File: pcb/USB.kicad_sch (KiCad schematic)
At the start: 103 parts, among them J0 12401598E4#2A, J2 1003-002-01100, J3 1003-002-01100, J4 12401598E4#2A, J5 12401598E4#2A, U0 USBLC6-2SC6, U10 AP22811AW5-7, U11 PTN5110NHQZ, U12 PTN5110NHQZ, U13 PTN5110NHQZ, U14 SN74LVC1G08DCKR, U15 CBTL02043ABQ,115, U19 SN74LVC1G08DCKR, U2 USB7006T/KDX, U20 AP22811AW5-7, U21 USBLC6-2SC6, U22 AP22811AW5-7, U23 AP22811AW5-7, U3 CBTL02043ABQ,115, U5 USBLC6-2SC6, U6 CBTL02043ABQ,115, U7 USBLC6-2SC6, U8 USBLC6-2SC6, U9 AP22811AW5-7, X1 ECS-3225MV-250-BN-TR

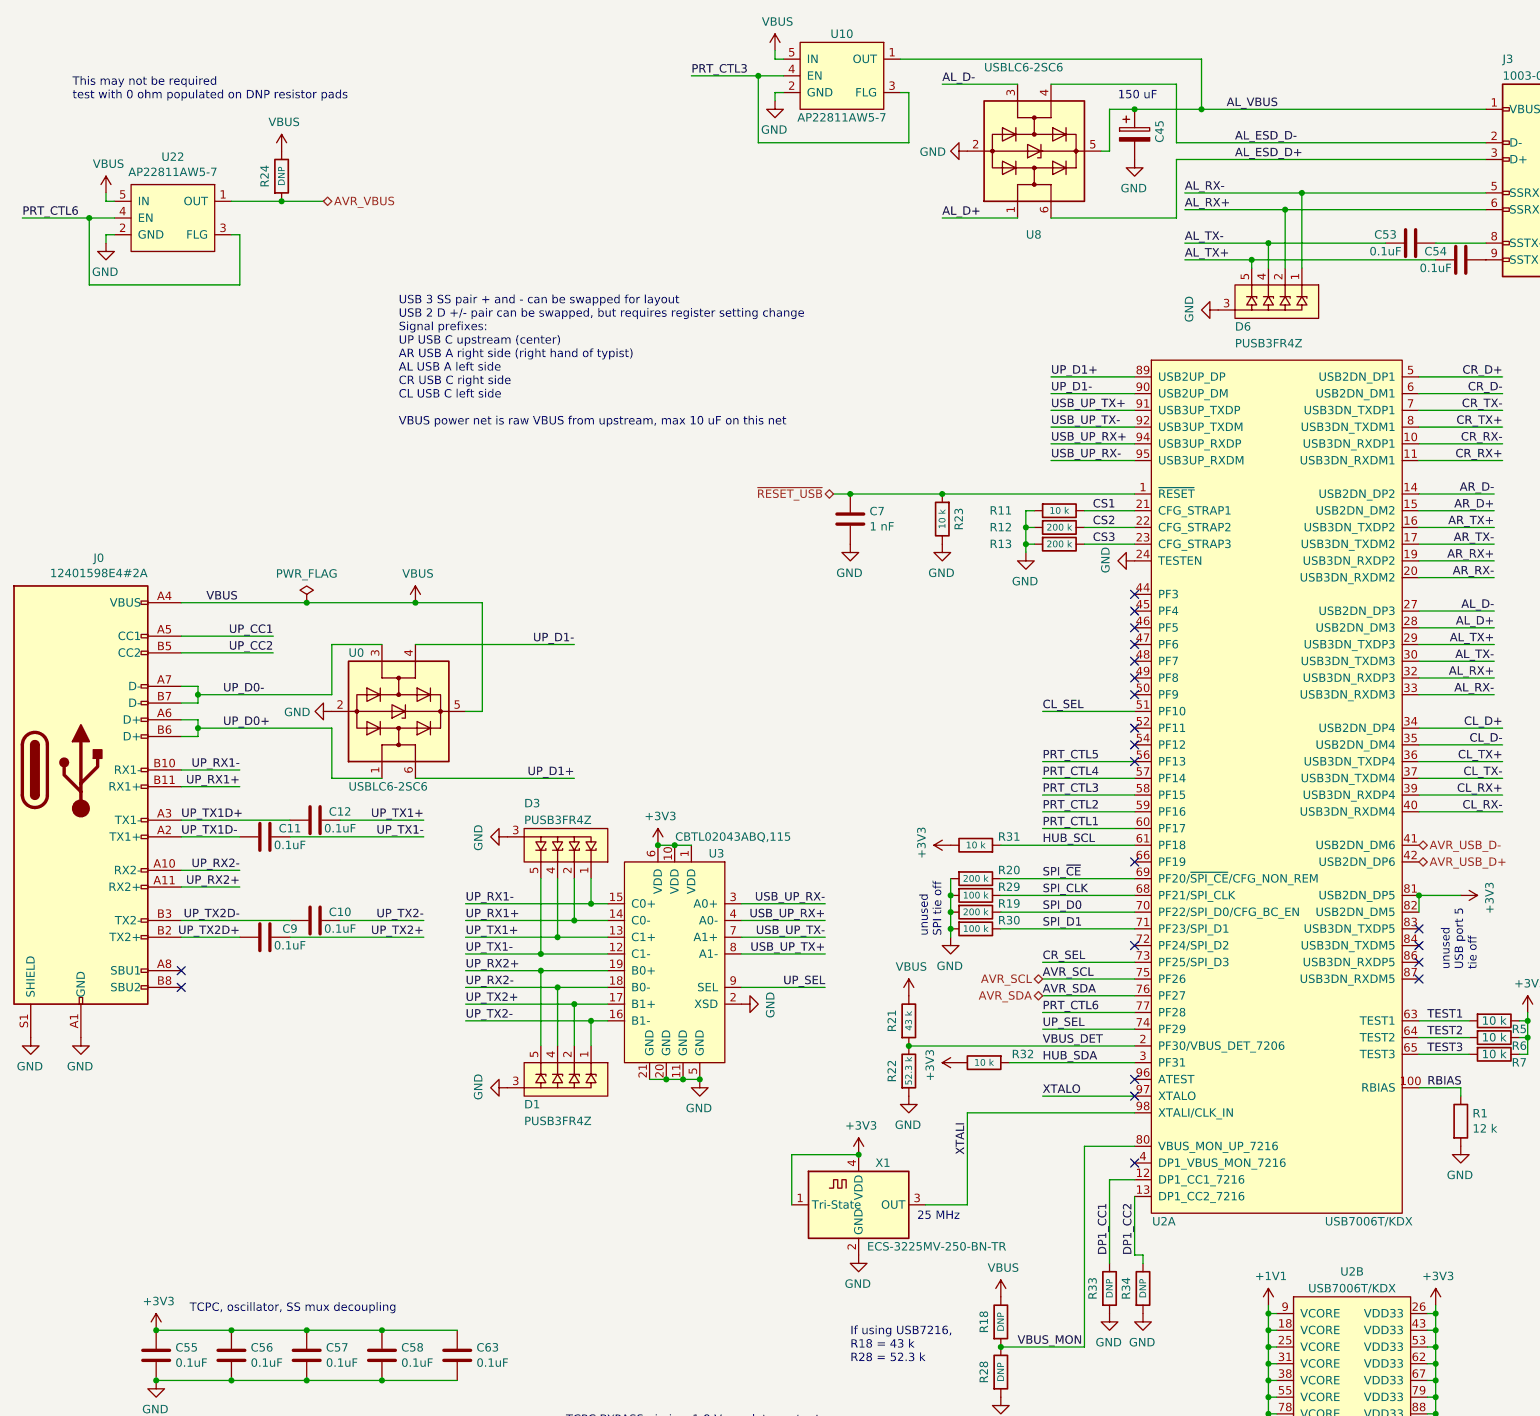
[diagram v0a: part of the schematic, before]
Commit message: RP2040, USB7216 Change USB hub part number to USB7216 Change microcontroller to RP2040 remove vbus switch for microcontroller as RP2040 does not require vbus sensing
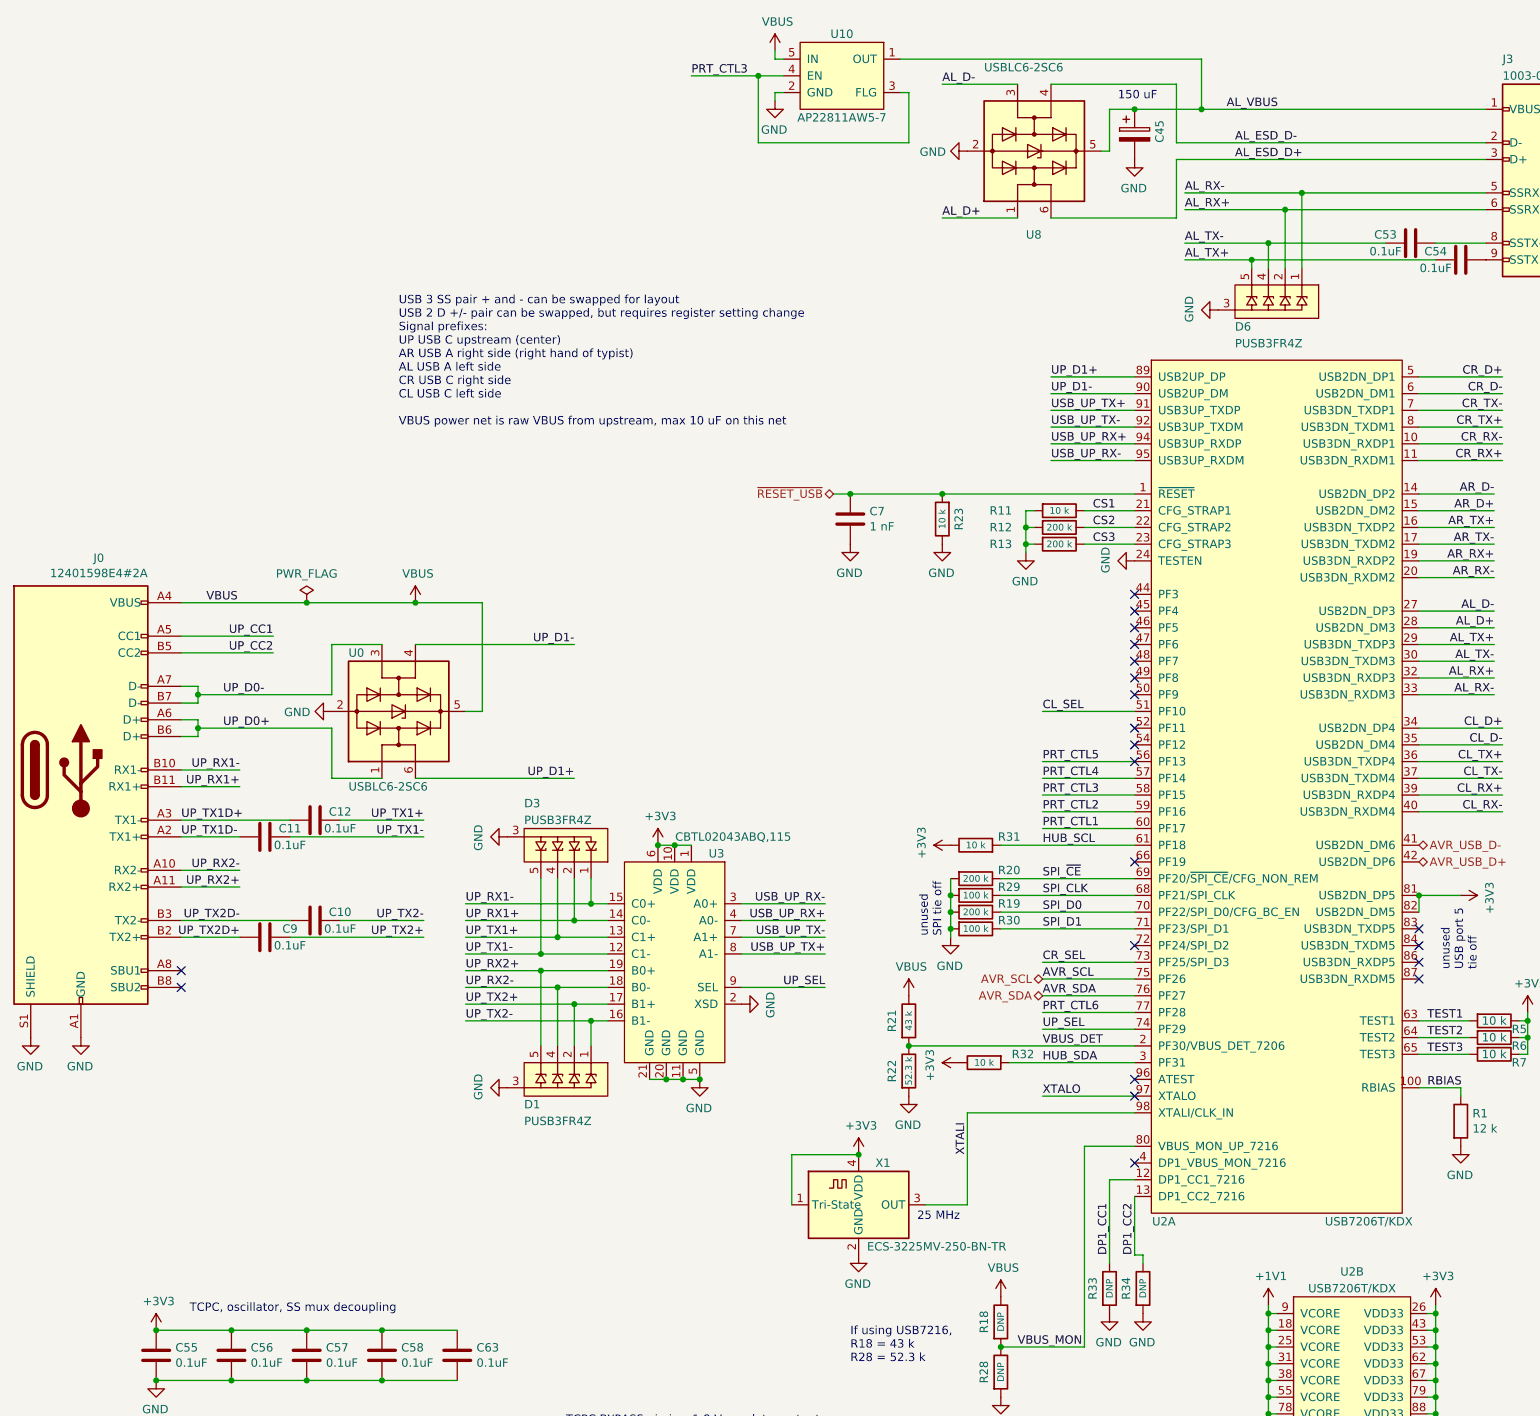
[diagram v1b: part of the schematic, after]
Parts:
- removed R24: DNP, launch:R_0402_1005Metric, symbol Device:R
- removed U22: AP22811AW5-7, launch:SOT-23-5, symbol launch:AP22811AW5-7‎
- U2: value USB7006T/KDX -> USB7206T/KDX
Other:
- note removed: "This may not be required test with 0 ohm populated on DNP resistor pads"
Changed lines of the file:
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@@
   (title_block
     (title "Launch")
-    (date "2022-05-24")
-    (rev "2.0")
+    (date "2023-01-31")
+    (rev "pre 3.0")
     (company "System76")
   )
@@
   (junction (at 29.21 266.7) (diameter 0) (color 0 0 0 0)
   )
-  (junction (at 58.42 41.91) (diameter 0) (color 0 0 0 0)
-  )
   (junction (at 208.28 218.44) (diameter 0) (color 0 0 0 0)
   )
@@
   (junction (at 209.55 257.81) (diameter 0) (color 0 0 0 0)
   )
-  (junction (at 29.21 44.45) (diameter 0) (color 0 0 0 0)
-  )
   (junction (at 243.84 250.19) (diameter 0) (color 0 0 0 0)
   )
@@
     (stroke (width 0) (type default))
   )
-  (wire (pts (xy 29.21 44.45) (xy 33.02 44.45))
-    (stroke (width 0) (type default))
-  )
   (wire (pts (xy 173.99 134.62) (xy 187.96 134.62))
     (stroke (width 0) (type default))
@@
     (stroke (width 0) (type default))
   )
-  (wire (pts (xy 52.07 46.99) (xy 50.8 46.99))
-    (stroke (width 0) (type default))
-  )
   (wire (pts (xy 290.83 172.72) (xy 289.56 172.72))
     (stroke (width 0) (type default))
@@
     (stroke (width 0) (type default))
   )
-  (wire (pts (xy 31.75 46.99) (xy 31.75 48.26))
-    (stroke (width 0) (type default))
-  )
   (wire (pts (xy 187.96 88.9) (xy 180.34 88.9))
     (stroke (width 0) (type default))
@@
     (stroke (width 0) (type default))
   )
-  (wire (pts (xy 33.02 41.91) (xy 31.75 41.91))
-    (stroke (width 0) (type default))
-  )
   (wire (pts (xy 363.22 36.83) (xy 345.44 36.83))
     (stroke (width 0) (type default))
@@
     (stroke (width 0) (type default))
   )
-  (wire (pts (xy 58.42 41.91) (xy 64.77 41.91))
-    (stroke (width 0) (type default))
-  )
   (wire (pts (xy 45.72 120.65) (xy 45.72 121.92))
     (stroke (width 0) (type default))
@@
     (stroke (width 0) (type default))
   )
-  (wire (pts (xy 29.21 54.61) (xy 52.07 54.61))
-    (stroke (width 0) (type default))
-  )
   (wire (pts (xy 233.68 220.98) (xy 233.68 223.52))
     (stroke (width 0) (type default))
@@
     (stroke (width 0) (type default))
   )
-  (wire (pts (xy 19.05 44.45) (xy 29.21 44.45))
-    (stroke (width 0) (type default))
-  )
-  (wire (pts (xy 31.75 41.91) (xy 31.75 40.64))
-    (stroke (width 0) (type default))
-  )
   (wire (pts (xy 175.26 81.28) (xy 187.96 81.28))
     (stroke (width 0) (type default))
@@
     (stroke (width 0) (type default))
   )
-  (wire (pts (xy 52.07 54.61) (xy 52.07 46.99))
-    (stroke (width 0) (type default))
-  )
   (wire (pts (xy 97.79 158.75) (xy 107.95 158.75))
     (stroke (width 0) (type default))
@@
     (stroke (width 0) (type default))
   )
-  (wire (pts (xy 33.02 46.99) (xy 31.75 46.99))
-    (stroke (width 0) (type default))
-  )
   (wire (pts (xy 194.31 35.56) (xy 194.31 44.45))
     (stroke (width 0) (type default))
@@
     (stroke (width 0) (type default))
   )
-  (wire (pts (xy 50.8 41.91) (xy 58.42 41.91))
-    (stroke (width 0) (type default))
-  )
   (wire (pts (xy 269.24 24.13) (xy 279.4 24.13))
     (stroke (width 0) (type default))
@@
     (stroke (width 0) (type default))
   )
-  (wire (pts (xy 29.21 44.45) (xy 29.21 54.61))
-    (stroke (width 0) (type default))
-  )
   (wire (pts (xy 259.08 57.15) (xy 259.08 55.88))
     (stroke (width 0) (type default))
@@
     (effects (font (size 1.27 1.27)) (justify left bottom))
   )
-  (text "This may not be required\ntest with 0 ohm populated on DNP resistor pads"
-    (at 26.67 26.67 0)
-    (effects (font (size 1.27 1.27)) (justify left bottom))
-  )
   (text "150 uF" (at 313.69 72.39 0)
     (effects (font (size 1.27 1.27)) (justify left bottom))
@@
     (effects (font (size 1.27 1.27)) (justify right bottom))
   )
-  (label "PRT_CTL6" (at 19.05 44.45 0) (fields_autoplaced)
-    (effects (font (size 1.27 1.27)) (justify left bottom))
-  )
   (label "CR_TX1+" (at 339.09 133.35 180) (fields_autoplaced)
     (effects (font (size 1.27 1.27)) (justify right bottom))
@@
     (effects (font (size 1.27 1.27)) (justify right))
   )
-  (hierarchical_label "AVR_VBUS" (shape bidirectional) (at 64.77 41.91 0) (fields_autoplaced)
-    (effects (font (size 1.27 1.27)) (justify left))
-  )
   (hierarchical_label "AVR_USB_D+" (shape bidirectional) (at 231.14 142.24 0) (fields_autoplaced)
     (effects (font (size 1.27 1.27)) (justify left))
@@
       (effects (font (size 1.27 1.27)))
     )
-    (property "Value" "USB7006T/KDX" (at 223.52 196.85 0)
+    (property "Value" "USB7206T/KDX" (at 223.52 196.85 0)
       (effects (font (size 1.27 1.27)))
     )
@@
       (effects (font (size 1.27 1.27)))
     )
-    (property "Value" "USB7006T/KDX" (at 220.98 207.01 0)
+    (property "Value" "USB7206T/KDX" (at 220.98 207.01 0)
       (effects (font (size 1.27 1.27)))
     )
@@
     )
   )
-  (symbol (lib_id "launch:AP22811AW5-7‎") (at 41.91 44.45 0) (unit 1)
-    (in_bom yes) (on_board yes) (dnp no)
-    (property "Reference" "U22" (at 41.91 35.179 0)
-      (effects (font (size 1.27 1.27)))
-    )
-    (property "Value" "AP22811AW5-7 " (at 41.91 37.4904 0)
-      (effects (font (size 1.27 1.27)))
-    )
-    (property "Footprint" "launch:SOT-23-5" (at 35.56 38.1 0)
-      (effects (font (size 1.27 1.27)) (justify left) hide)
-    )
-    (property "Datasheet" "${KIPRJMOD}/docs/AP22811.pdf" (at 41.91 39.37 90)
-      (effects (font (size 1.27 1.27)) hide)
-    )
-    (property "Manufacturer" "Diodes Inc." (at 41.91 44.45 0)
-      (effects (font (size 1.27 1.27)) hide)
-    )
-    (pin "1")
-    (pin "2")
-    (pin "3")
-    (pin "4")
-    (pin "5")
-    (instances
-      (project "launch"
-        (path "/80c969df-cd39-4c4a-8336-5a366308cfd3/00000000-0000-0000-0000-00005f58df7c"
-          (reference "U22") (unit 1)
-        )
-      )
-    )
-  )
-  (symbol (lib_id "power:GND") (at 31.75 48.26 0) (mirror y) (unit 1)
-    (in_bom yes) (on_board yes) (dnp no)
-    (property "Reference" "#PWR0112" (at 31.75 54.61 0)
-      (effects (font (size 1.27 1.27)) hide)
-    )
-    (property "Value" "GND" (at 31.623 52.6542 0)
-      (effects (font (size 1.27 1.27)))
-    )
-    (property "Footprint" "" (at 31.75 48.26 0)
-      (effects (font (size 1.27 1.27)) hide)
-    )
-    (property "Datasheet" "" (at 31.75 48.26 0)
-      (effects (font (size 1.27 1.27)) hide)
-    )
-    (pin "1")
-    (instances
-      (project "launch"
-        (path "/80c969df-cd39-4c4a-8336-5a366308cfd3/00000000-0000-0000-0000-00005f58df7c"
-          (reference "#PWR0112") (unit 1)
-        )
-      )
-    )
-  )
-  (symbol (lib_id "power:VBUS") (at 31.75 40.64 0) (unit 1)
-    (in_bom yes) (on_board yes) (dnp no)
-    (property "Reference" "#PWR0214" (at 31.75 44.45 0)
-      (effects (font (size 1.27 1.27)) hide)
-    )
-    (property "Value" "VBUS" (at 32.131 36.2458 0)
-      (effects (font (size 1.27 1.27)))
-    )
-    (property "Footprint" "" (at 31.75 40.64 0)
-      (effects (font (size 1.27 1.27)) hide)
-    )
-    (property "Datasheet" "" (at 31.75 40.64 0)
-      (effects (font (size 1.27 1.27)) hide)
-    )
-    (pin "1")
-    (instances
-      (project "launch"
-        (path "/80c969df-cd39-4c4a-8336-5a366308cfd3/00000000-0000-0000-0000-00005f58df7c"
-          (reference "#PWR0214") (unit 1)
-        )
-      )
-    )
-  )
   (symbol (lib_id "power:VBUS") (at 78.74 102.87 0) (unit 1)
     (in_bom yes) (on_board yes) (dnp no)
@@
         )
       )
-    )
-  )
-  (symbol (lib_id "power:VBUS") (at 58.42 34.29 0) (unit 1)
-    (in_bom yes) (on_board yes) (dnp no)
-    (property "Reference" "#PWR0197" (at 58.42 38.1 0)
-      (effects (font (size 1.27 1.27)) hide)
-    )
-    (property "Value" "VBUS" (at 58.801 29.8958 0)
-      (effects (font (size 1.27 1.27)))
-    )
-    (property "Footprint" "" (at 58.42 34.29 0)
-      (effects (font (size 1.27 1.27)) hide)
-    )
-    (property "Datasheet" "" (at 58.42 34.29 0)
-      (effects (font (size 1.27 1.27)) hide)
-    )
-    (pin "1")
-    (instances
-      (project "launch"
-        (path "/80c969df-cd39-4c4a-8336-5a366308cfd3/00000000-0000-0000-0000-00005f58df7c"
-          (reference "#PWR0197") (unit 1)
-        )
-      )
-    )
-  )
-  (symbol (lib_id "Device:R") (at 58.42 38.1 0) (unit 1)
-    (in_bom yes) (on_board yes) (dnp no)
-    (property "Reference" "R24" (at 55.88 38.1 90)
-      (effects (font (size 1.27 1.27)))
-    )
-    (property "Value" "DNP" (at 58.42 38.1 90)
-      (effects (font (size 1.016 1.016)))
-    )
-    (property "Footprint" "launch:R_0402_1005Metric" (at 56.642 38.1 90)
-      (effects (font (size 1.27 1.27)) hide)
-    )
-    (property "Datasheet" "~" (at 58.42 38.1 0)
-      (effects (font (size 1.27 1.27)) hide)
-    )
-    (property "Manufacturer" "Generic 1% resistor" (at 58.42 38.1 0)
-      (effects (font (size 1.27 1.27)) hide)
-    )
-    (pin "1")
-    (pin "2")
-    (instances
-      (project "launch"
-        (path "/80c969df-cd39-4c4a-8336-5a366308cfd3/00000000-0000-0000-0000-00005f58df7c"
-          (reference "R24") (unit 1)
-        )
-      )

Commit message: change AVR to UC on some net names since we don't have an Atmel AVR controller now
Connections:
- net AVR_SCL renamed UC_SCL
- net AVR_SDA renamed UC_SDA
- net AVR_USB_D+ renamed UC_USB_D+
- net AVR_USB_D- renamed UC_USB_D-
- no-connect marks 42 -> 43
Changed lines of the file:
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@@
   (title_block
     (title "Launch")
-    (date "2023-01-31")
+    (date "2023-02-03")
     (rev "pre 3.0")
     (company "System76")
@@
   (no_connect (at 180.34 251.46))
   (no_connect (at 379.73 226.06))
+  (no_connect (at 187.96 165.1))
   (no_connect (at 187.96 111.76))
   (no_connect (at 118.11 261.62))
@@
     (effects (font (size 1.27 1.27)) (justify right bottom))
   )
+  (label "UC_SCL" (at 173.99 160.02 0) (fields_autoplaced)
+    (effects (font (size 1.27 1.27)) (justify left bottom))
+  )
   (label "UP_RX1+" (at 52.07 130.81 180) (fields_autoplaced)
     (effects (font (size 1.27 1.27)) (justify right bottom))
@@
     (effects (font (size 1.27 1.27)) (justify left bottom))
   )
-  (label "AVR_SDA" (at 27.94 261.62 0) (fields_autoplaced)
+  (label "UC_SDA" (at 27.94 261.62 0) (fields_autoplaced)
     (effects (font (size 1.27 1.27)) (justify left bottom))
   )
@@
     (effects (font (size 1.27 1.27)) (justify right bottom))
   )
-  (label "AVR_SCL" (at 173.99 160.02 0) (fields_autoplaced)
-    (effects (font (size 1.27 1.27)) (justify left bottom))
-  )
   (label "CL_VBUS" (at 365.76 167.64 0) (fields_autoplaced)
     (effects (font (size 1.27 1.27)) (justify left bottom))
@@
     (effects (font (size 1.27 1.27)) (justify right bottom))
   )
-  (label "AVR_SCL" (at 85.09 259.08 0) (fields_autoplaced)
+  (label "UC_SCL" (at 85.09 259.08 0) (fields_autoplaced)
     (effects (font (size 1.27 1.27)) (justify left bottom))
   )
@@
     (effects (font (size 1.27 1.27)) (justify left bottom))
   )
-  (label "AVR_SDA" (at 85.09 261.62 0) (fields_autoplaced)
+  (label "UC_SDA" (at 85.09 261.62 0) (fields_autoplaced)
     (effects (font (size 1.27 1.27)) (justify left bottom))
   )
@@
     (effects (font (size 1.27 1.27)) (justify left bottom))
   )
-  (label "AVR_SCL" (at 147.32 259.08 0) (fields_autoplaced)
+  (label "UC_SCL" (at 147.32 259.08 0) (fields_autoplaced)
     (effects (font (size 1.27 1.27)) (justify left bottom))
   )
@@
     (effects (font (size 1.27 1.27)) (justify left bottom))
   )
+  (label "UC_SDA" (at 173.99 162.56 0) (fields_autoplaced)
+    (effects (font (size 1.27 1.27)) (justify left bottom))
+  )
   (label "HUB_SCL" (at 173.99 139.7 0) (fields_autoplaced)
     (effects (font (size 1.27 1.27)) (justify left bottom))
   )
-  (label "AVR_SDA" (at 147.32 261.62 0) (fields_autoplaced)
+  (label "UC_SDA" (at 147.32 261.62 0) (fields_autoplaced)
     (effects (font (size 1.27 1.27)) (justify left bottom))
   )
@@
     (effects (font (size 1.27 1.27)) (justify right bottom))
   )
-  (label "AVR_SDA" (at 173.99 162.56 0) (fields_autoplaced)
-    (effects (font (size 1.27 1.27)) (justify left bottom))
-  )
   (label "DP1_CC1" (at 184.15 201.93 90) (fields_autoplaced)
     (effects (font (size 1.27 1.27)) (justify left bottom))
@@
     (effects (font (size 1.27 1.27)) (justify left bottom))
   )
-  (label "AVR_SCL" (at 27.94 259.08 0) (fields_autoplaced)
+  (label "UC_SCL" (at 27.94 259.08 0) (fields_autoplaced)
     (effects (font (size 1.27 1.27)) (justify left bottom))
   )
@@
     (effects (font (size 1.27 1.27)) (justify right bottom))
   )
-  (hierarchical_label "AVR_USB_D-" (shape bidirectional) (at 231.14 139.7 0) (fields_autoplaced)
+  (hierarchical_label "UC_USB_D-" (shape bidirectional) (at 231.14 139.7 0) (fields_autoplaced)
     (effects (font (size 1.27 1.27)) (justify left))
   )
-  (hierarchical_label "AVR_SCL" (shape bidirectional) (at 173.99 160.02 180) (fields_autoplaced)
+  (hierarchical_label "UC_SCL" (shape bidirectional) (at 173.99 160.02 180) (fields_autoplaced)
     (effects (font (size 1.27 1.27)) (justify right))
   )
-  (hierarchical_label "AVR_SDA" (shape bidirectional) (at 173.99 162.56 180) (fields_autoplaced)
+  (hierarchical_label "UC_SDA" (shape bidirectional) (at 173.99 162.56 180) (fields_autoplaced)
     (effects (font (size 1.27 1.27)) (justify right))
   )
@@
     (effects (font (size 1.27 1.27)) (justify right))
   )
-  (hierarchical_label "AVR_USB_D+" (shape bidirectional) (at 231.14 142.24 0) (fields_autoplaced)
+  (hierarchical_label "UC_USB_D+" (shape bidirectional) (at 231.14 142.24 0) (fields_autoplaced)
     (effects (font (size 1.27 1.27)) (justify left))
   )
